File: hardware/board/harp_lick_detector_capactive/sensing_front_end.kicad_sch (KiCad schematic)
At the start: 29 parts

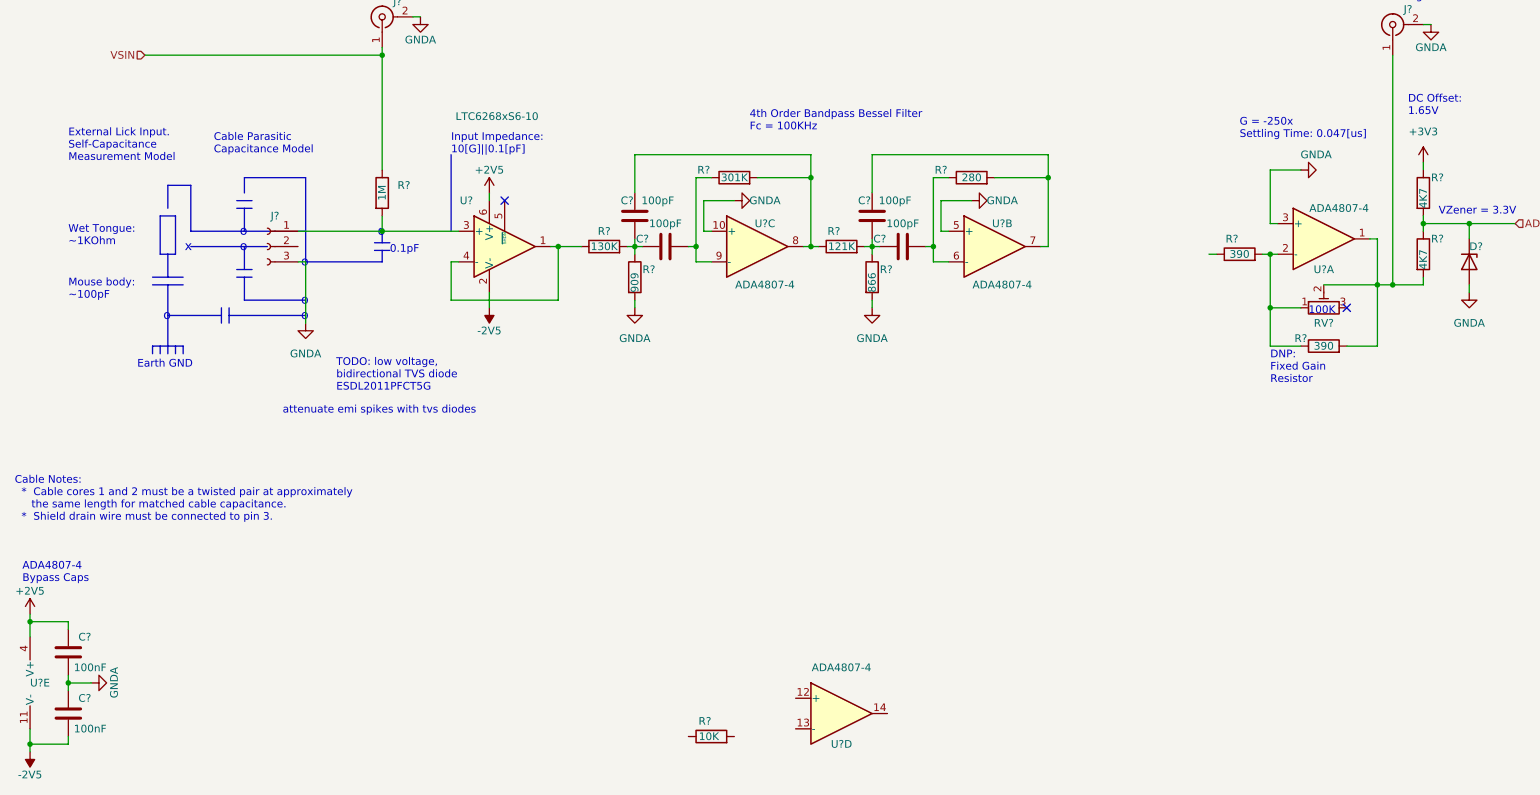
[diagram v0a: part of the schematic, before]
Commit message: add extra series termination resistors
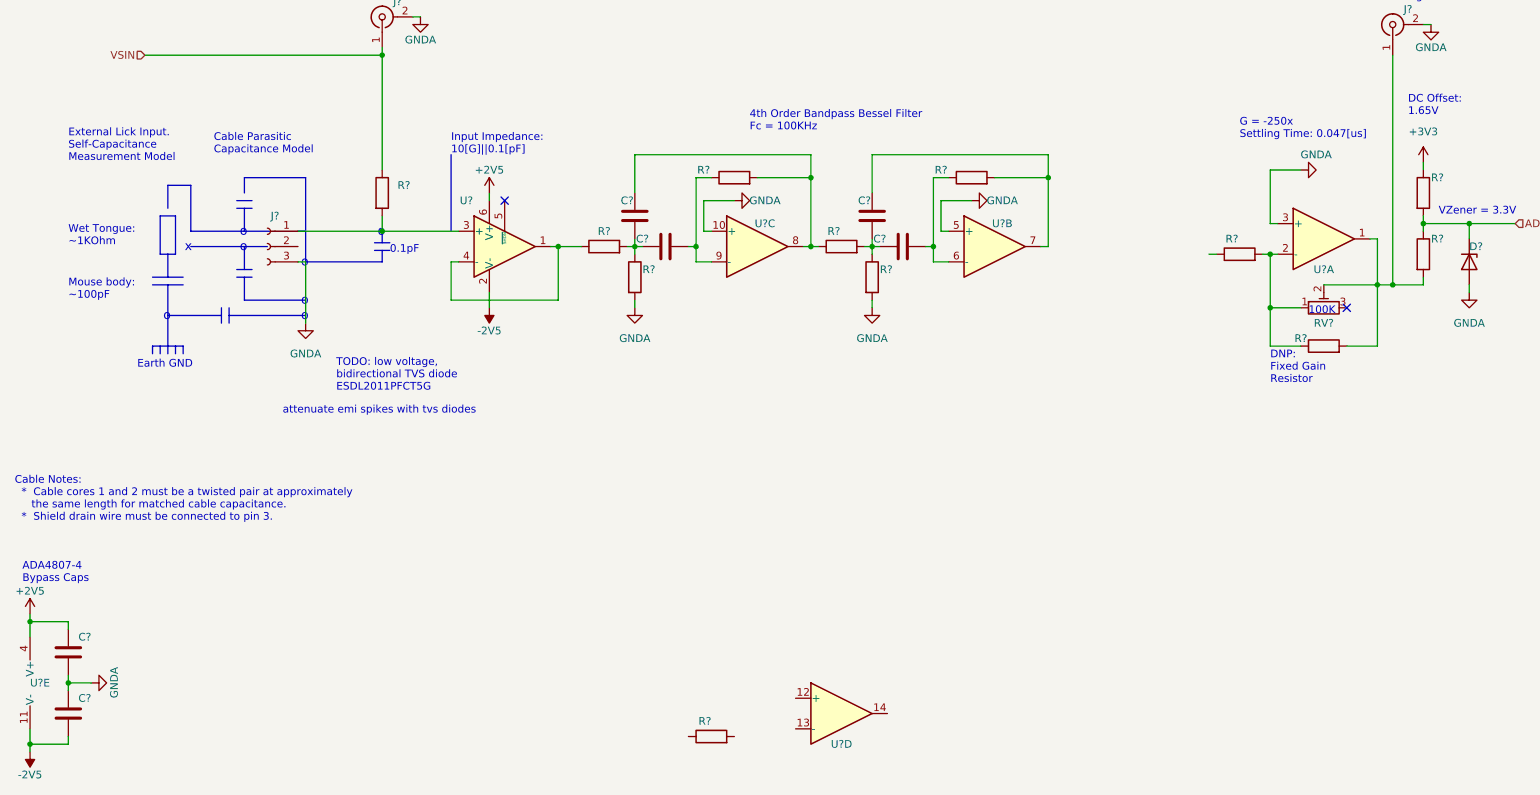
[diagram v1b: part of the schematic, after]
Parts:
- C? (x2): value 100nF -> (none); footprint Capacitor_SMD:C_0603_1608Metric_Pad1.08x0.95mm_HandSolder -> (none)
- C? (x4): value 100pF -> (none); footprint Capacitor_SMD:C_0603_1608Metric_Pad1.08x0.95mm_HandSolder -> (none)
- D?: value BZX384-A3V3-QX -> (none); footprint Diode_SMD:D_SOD-323_HandSoldering -> (none)
- J? (x2): value Conn_Coaxial -> (none); footprint Connector_Coaxial:SMA_Amphenol_901-143_Horizontal -> (none)
- J?: value 3-Pin Connector Socket -> (none); footprint Connector_Phoenix_MC:PhoenixContact_MC_1,5_3-G-3.5_1x03_P3.50mm_Horizontal -> (none)
- R?: value 10K -> (none); footprint Resistor_SMD:R_0402_1005Metric_Pad0.72x0.64mm_HandSolder -> (none)
- R?: value 1M -> (none); Link (none) -> https://www.digikey.com/en/products/detail/te-connectivity-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; Manufacturer (none) -> TE Connectivity Passive Product; Manufacturer Number (none) -> CRGP0603F1M0
- R?: value 909 -> (none)
- R? (x2): value 4K7 -> (none); footprint Resistor_SMD:R_0603_1608Metric_Pad0.98x0.95mm_HandSolder -> (none)
- R? (x2): value 390 -> (none); footprint Resistor_SMD:R_0603_1608Metric_Pad0.98x0.95mm_HandSolder -> (none)
- R?: value 866 -> (none)
- R?: value 121K -> (none)
- R?: value 130K -> (none)
- R?: value 301K -> (none)
- R?: value 280 -> (none)
- RV?: value R_Potentiometer_Trim -> (none); footprint Potentiometer_SMD:Potentiometer_Bourns_3314G_Vertical -> (none)
- U? (x5): value ADA4807-4 -> (none); footprint Package_SO:TSSOP-14_4.4x5mm_P0.65mm -> (none)
- U?: value LTC6268xS6-10 -> (none)

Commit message: add driven shield
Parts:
- removed C? (x3): (no value), symbol Device:C
- removed J?: (no value), symbol Connector:Conn_01x03_Female
- removed R? (x7): (no value), symbol Device:R
- added C? (x3): 100pF, Capacitor_SMD:C_0603_1608Metric_Pad1.08x0.95mm_HandSolder, symbol Device:C
- added C?: 1nF, symbol Device:C
- added C?: 5.6nF, symbol Device:C
- added C?: 270pF, symbol Device:C
- added J?: (no value), symbol Connector:Conn_01x02_Female
- added R? (x3): (no value), symbol Device:R
- added R?: 13K3, symbol Device:R
- added R? (x2): 15K8, symbol Device:R
- added R?: 25K5, symbol Device:R
- added R?: 1M, Resistor_SMD:R_0603_1608Metric_Pad0.98x0.95mm_HandSolder, symbol Device:R
- added R?: 1K54, symbol Device:R
- added R?: 3K01, symbol Device:R
- added U? (x2): ADA4807-4, Package_SO:TSSOP-14_4.4x5mm_P0.65mm, symbol Amplifier_Operational:ADA4807-4
- C? (x2): value (none) -> 100nF; footprint (none) -> Capacitor_SMD:C_0603_1608Metric_Pad1.08x0.95mm_HandSolder
- C?: value (none) -> 100pF; footprint (none) -> Capacitor_SMD:C_0603_1608Metric_Pad1.08x0.95mm_HandSolder
- D?: value (none) -> BZX384-A3V3-QX; footprint (none) -> Diode_SMD:D_SOD-323_HandSoldering
- J? (x2): value (none) -> Conn_Coaxial; footprint (none) -> Connector_Coaxial:SMA_Amphenol_901-143_Horizontal
- R?: value (none) -> 1M; footprint (none) -> Resistor_SMD:R_0603_1608Metric_Pad0.98x0.95mm_HandSolder
- R? (x2): value (none) -> 4K7; footprint (none) -> Resistor_SMD:R_0603_1608Metric_Pad0.98x0.95mm_HandSolder
- R? (x2): value (none) -> 390; footprint (none) -> Resistor_SMD:R_0603_1608Metric_Pad0.98x0.95mm_HandSolder
- RV?: value (none) -> R_Potentiometer_Trim; footprint (none) -> Potentiometer_SMD:Potentiometer_Bourns_3314G_Vertical
- U? (x5): value (none) -> ADA4807-4; footprint (none) -> Package_SO:TSSOP-14_4.4x5mm_P0.65mm
- U?: value (none) -> LTC6268xS6-10
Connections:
- net GNDA: now also C?.1, C?.1, C?.1, R?.1, R?.2; no longer U?.10 (+), U?.5 (+)
- net VSIN: now also J?.2 (Pin_2)
- net at U?.6 (-): now also R?.1
- net at U?.3 (+): no longer R?.2
- net at U?.8: now also U?.9 (-), C?.2, R?.1
- net at C?.2: now also U?.10 (+), R?.1; no longer U?.7
- net at U?.12 (+): now also C?.2, R?.1
- net at U?.13 (-): now also R?.1
- net at U?.14: now also R?.2
- new net: C?.2, R?.2, U?.12 (+)
- new net: C?.2, U?.13 (-), U?.14
- new net: C?.1, R?.2, U?.10 (+)
- new net: C?.1, R?.2, R?.2
- new net: C?.2, C?.2, R?.1, R?.2
- new net: J?.1 (Pin_1), R?.2, U?.5 (+)
- new net: C?.1, R?.2, U?.7
- new net: C?.1, R?.1, R?.2
- new net: R?.2, U?.8, U?.9 (-)
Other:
- note added: "1pF"
- note added: "1st Order Highpass Filter w/input bias current compensation. Fc = 10KHz"
- note added: "2nd Order Bandpass Filter, Bessel Fc = 100KHz"
- note added: "2nd Order lowpass filter, inverting, Chebyshev Fc = 100KHz"
- note added: "4th Order Lowpass Filter, Chebyshev Fc = 100KHz"
- note added: "Buffer w/input bias current compensation."
- note added: "Cable Notes: Cable should be either: * a coax cable (ideal) * a twisted pair"
- note added: "Driven shield removes parasitic capacitance from cable."
- note removed: "0.1pF"
- note removed: "4th Order Bandpass Bessel Filter Fc = 100KHz"
- note removed: "Cable Notes: * Cable cores 1 and 2 must be a twisted pair at approximately the same length for matched cable capacitance. * Shield drain wire must be connected to pin 3."
- note removed: "Cable Parasitic Capacitance Model"
- note removed: "attenuate emi spikes with tvs diodes"
- moved on the sheet: C?, D?, J?, R?, RV?, U?, U?A, U?B, U?C, U?D, U?E

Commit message: capture benchtop version
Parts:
- removed C? (x2): 100pF, Capacitor_SMD:C_0603_1608Metric_Pad1.08x0.95mm_HandSolder, symbol Device:C
- removed R? (x3): (no value), symbol Device:R
- removed U? (x2): ADA4807-4, Package_SO:TSSOP-14_4.4x5mm_P0.65mm, symbol Amplifier_Operational:ADA4807-4
- added C?: 100pF, Capacitor_SMD:C_0603_1608Metric_Pad1.08x0.95mm_HandSolder, symbol Device:C
- added R?: 2K7, symbol Device:R
- added U?: ADA4807-4, Package_SO:TSSOP-14_4.4x5mm_P0.65mm, symbol Amplifier_Operational:ADA4807-4
- J?: value (none) -> Conn_01x02_Female
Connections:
- net GNDA: now also C?.1
- net at R?.1: now also U?.9 (-)
- net at R?.2: now also U?.8
- net at C?.2, R?.1: now also U?.10 (+)
- new net: C?.2, R?.2
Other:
- note added: "Do we need to bias the lowpass filter? https://www.daenotes.com/electronics/devices-circuits/operational-amplifier-bias-current-compensation-method"
- note added: "FIXME: replace ADA4807 with OPA4354AQPWRQ1 with has ~3pA input bias current"
- note added: "Input Impedance: 45[M]||1[pF]"
- note removed: "2nd Order Bandpass Filter, Bessel Fc = 100KHz"
- moved on the sheet: J?
